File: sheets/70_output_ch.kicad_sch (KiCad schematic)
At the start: 21 parts, among them Q701 DMN10H220LQ, Q702 BC817-40, Q703 BC807-40, U701 74AHCT1G126

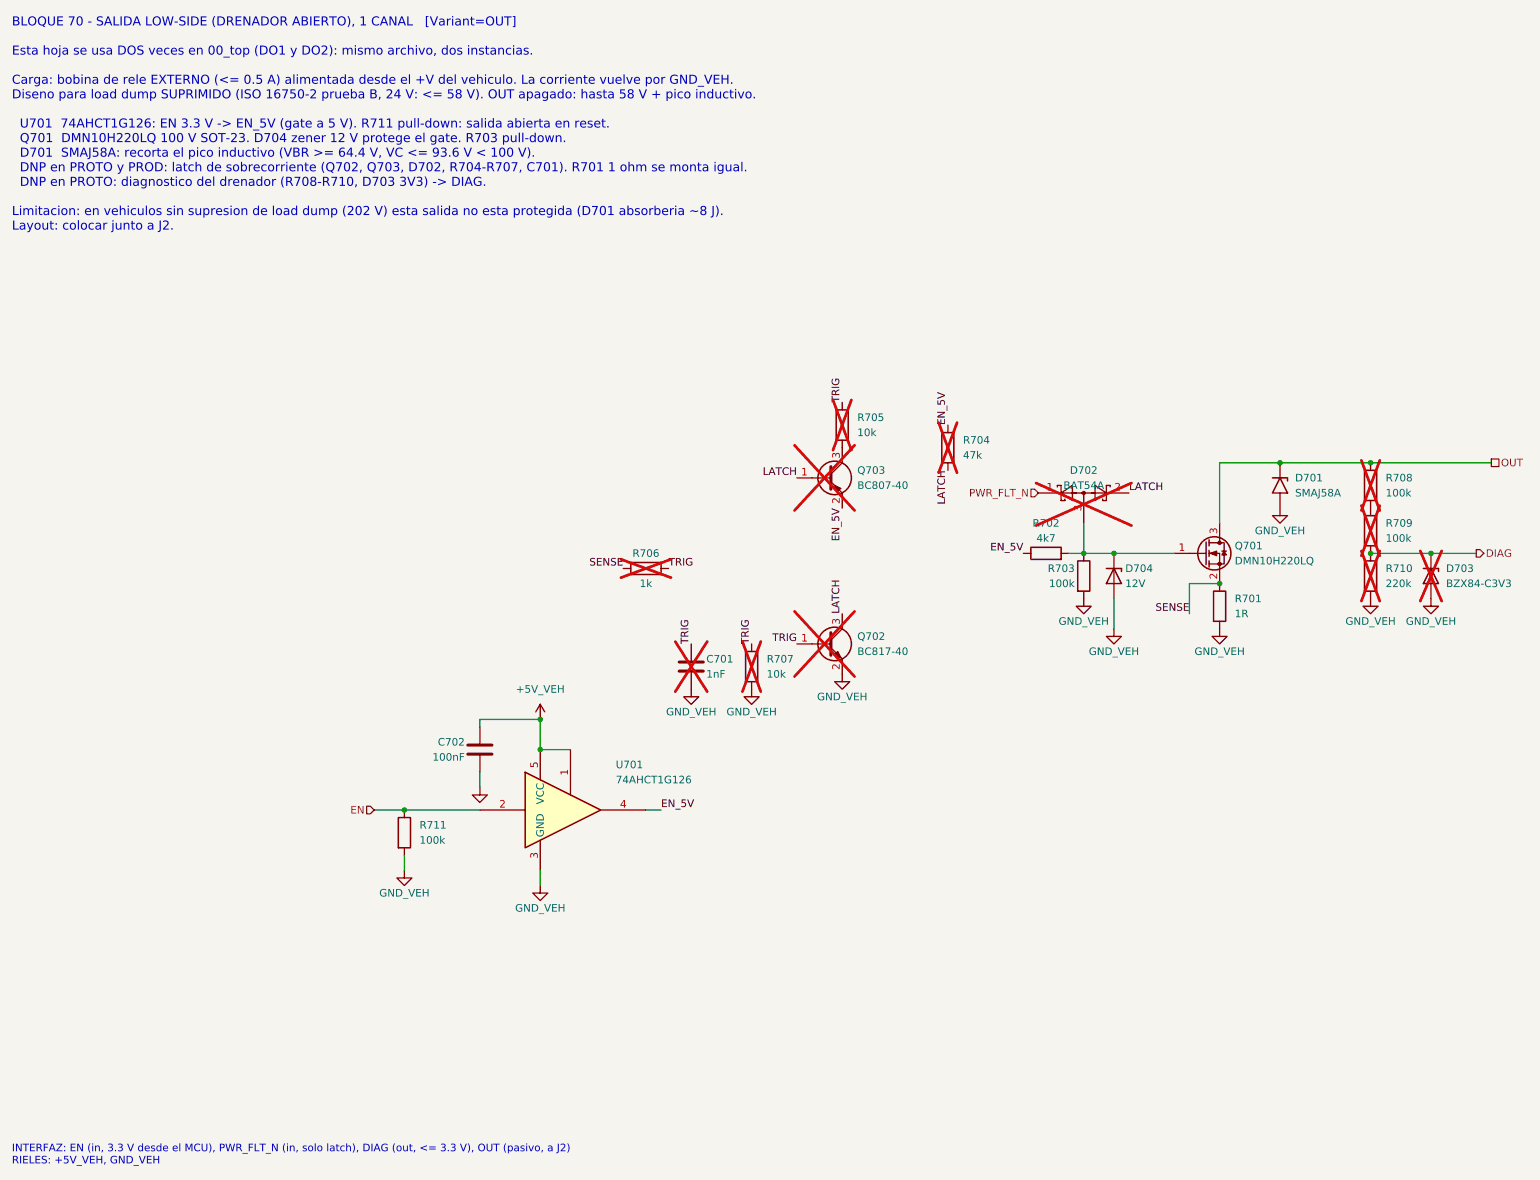
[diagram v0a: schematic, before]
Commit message: [Claude Code] 70_output: retira latch de sobrecorriente y R701/R751; borra propuesta 120x80
- 70_output_ch (DO1/DO2): fuera Q702/Q703, D702, R704-R707, C701 y R701
  (y equivalentes 75x). Fuente de Q701 directo a GND_VEH. PWR_FLT_N deja de
  entrar a la hoja 70 (pin jerarquico y conexiones de la raiz retirados).
  Se conserva el diagnostico (DNP en PROTO).
- ERC 0 errores / 1 aviso conocido. Paridad con la propuesta 100x100:
  22 diferencias esperadas, pendiente Update PCB from Schematic.
- docs/layout: se borra la propuesta 120x80 (recuperable de aa0a41b).

Co-Authored-By: Claude Opus 5.5 <noreply@anthropic.com>
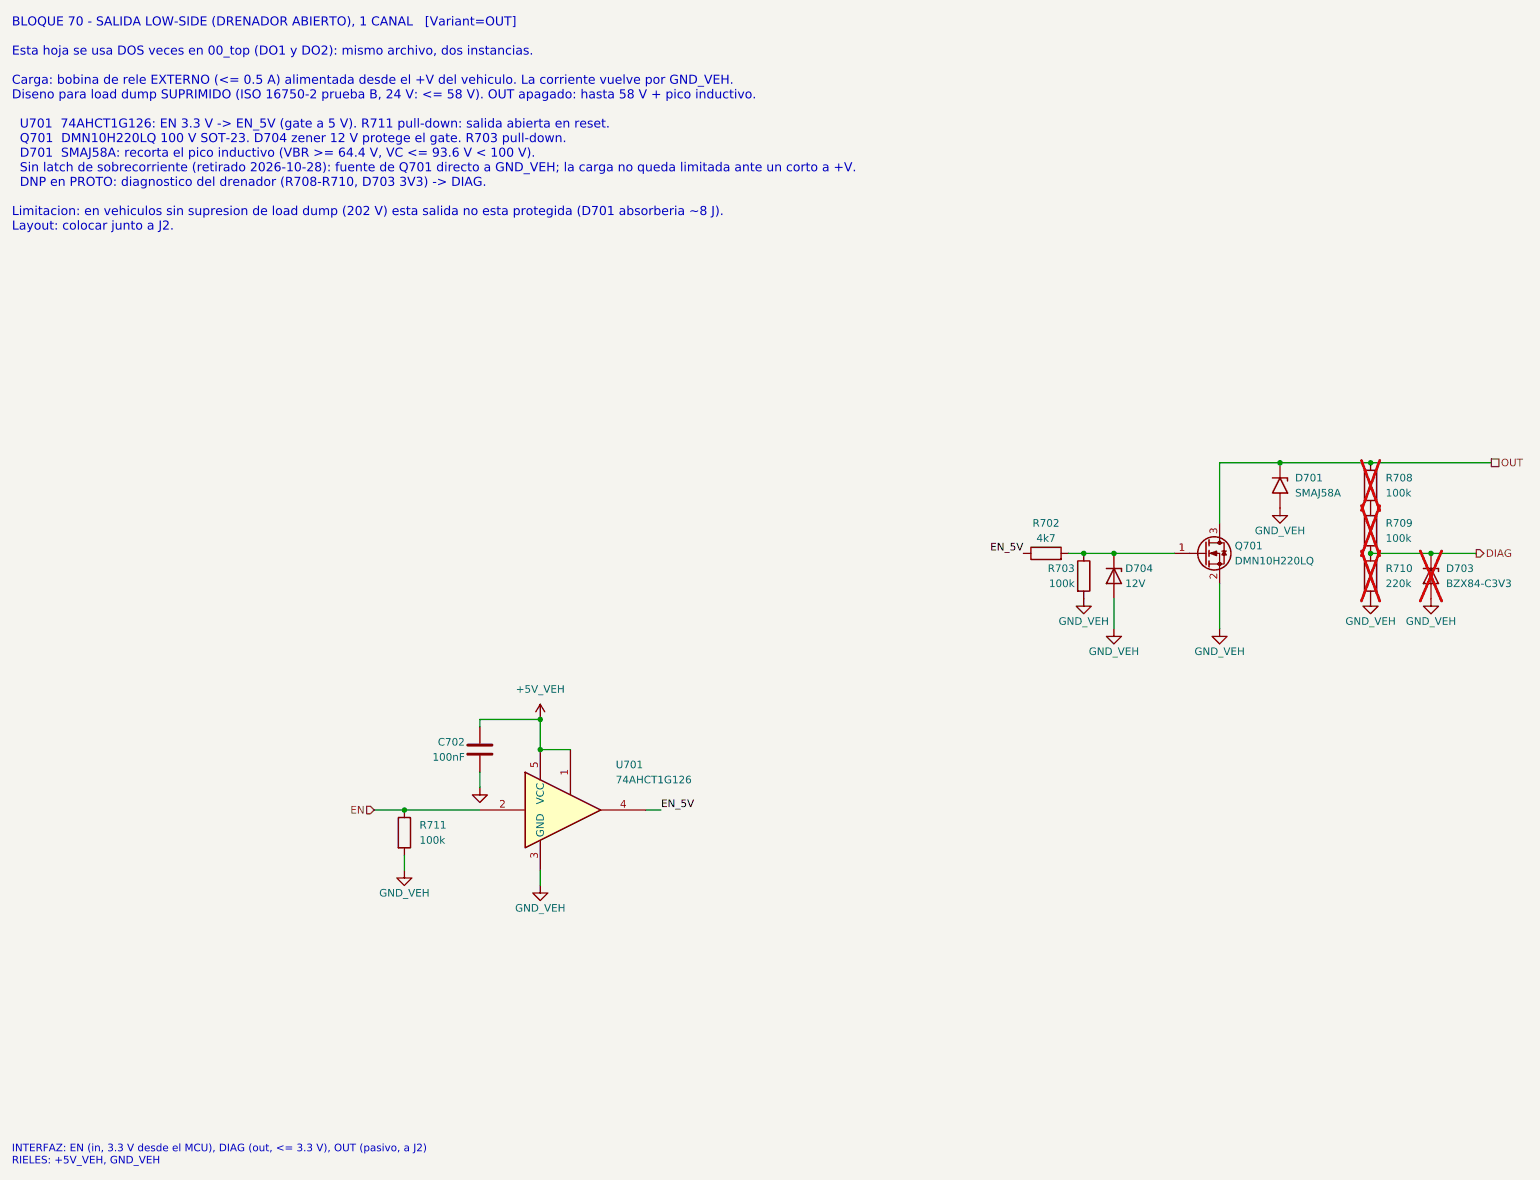
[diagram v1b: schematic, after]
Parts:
- removed C701: 1nF, Capacitor_SMD:C_0603_1608Metric, symbol Device:C
- removed D702: BAT54A, Package_TO_SOT_SMD:SOT-23, symbol Diode:BAT54A
- removed Q702: BC817-40, Package_TO_SOT_SMD:SOT-23, symbol Transistor_BJT:Q_NPN_BEC
- removed Q703: BC807-40, Package_TO_SOT_SMD:SOT-23, symbol Transistor_BJT:Q_PNP_BEC
- removed R701: 1R, Resistor_SMD:R_1206_3216Metric, symbol Device:R
- removed R704: 47k, Resistor_SMD:R_0603_1608Metric, symbol Device:R
- removed R705, R707: 10k, Resistor_SMD:R_0603_1608Metric, symbol Device:R
- removed R706: 1k, Resistor_SMD:R_0603_1608Metric, symbol Device:R
- R702: Notes Gate en serie: limita la corriente de carga del gate y deja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 -> Gate en serie: limita la corriente de carga del gate desde 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
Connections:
- net SENSE is gone; now on net GND_VEH: Q701.2 (S)
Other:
- note added: "INTERFAZ: EN (in, 3.3 V desde el MCU), DIAG (out, <= 3.3 V), OUT (pasivo, a J2) RIELES: +5V_VEH, GND_VEH"
- note removed: "INTERFAZ: EN (in, 3.3 V desde el MCU), PWR_FLT_N (in, solo latch), DIAG (out, <= 3.3 V), OUT (pasivo, a J2) RIELES: +5V_VEH, GND_VEH"
